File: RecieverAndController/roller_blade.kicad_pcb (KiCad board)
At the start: 2 copper layers, 57 x 60.4 mm, 2 parts

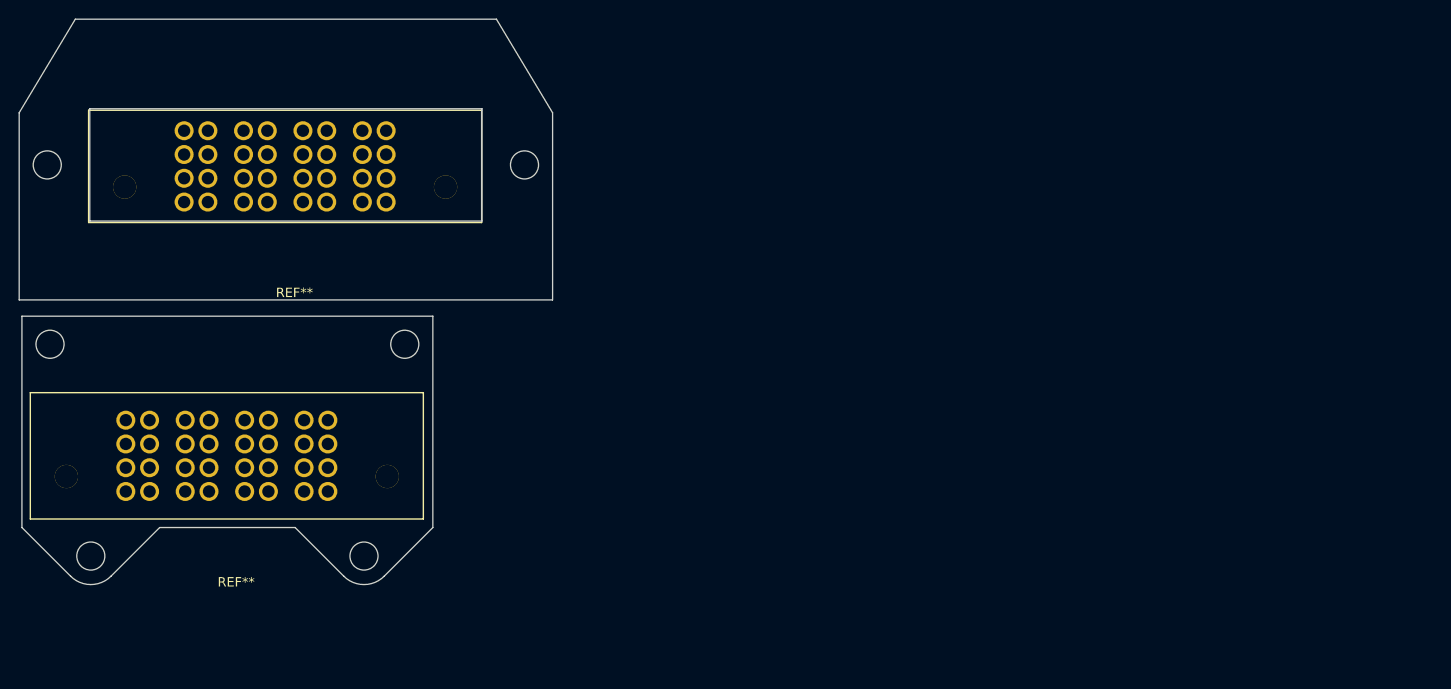
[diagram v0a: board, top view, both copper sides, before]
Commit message: adding footprints to schematic
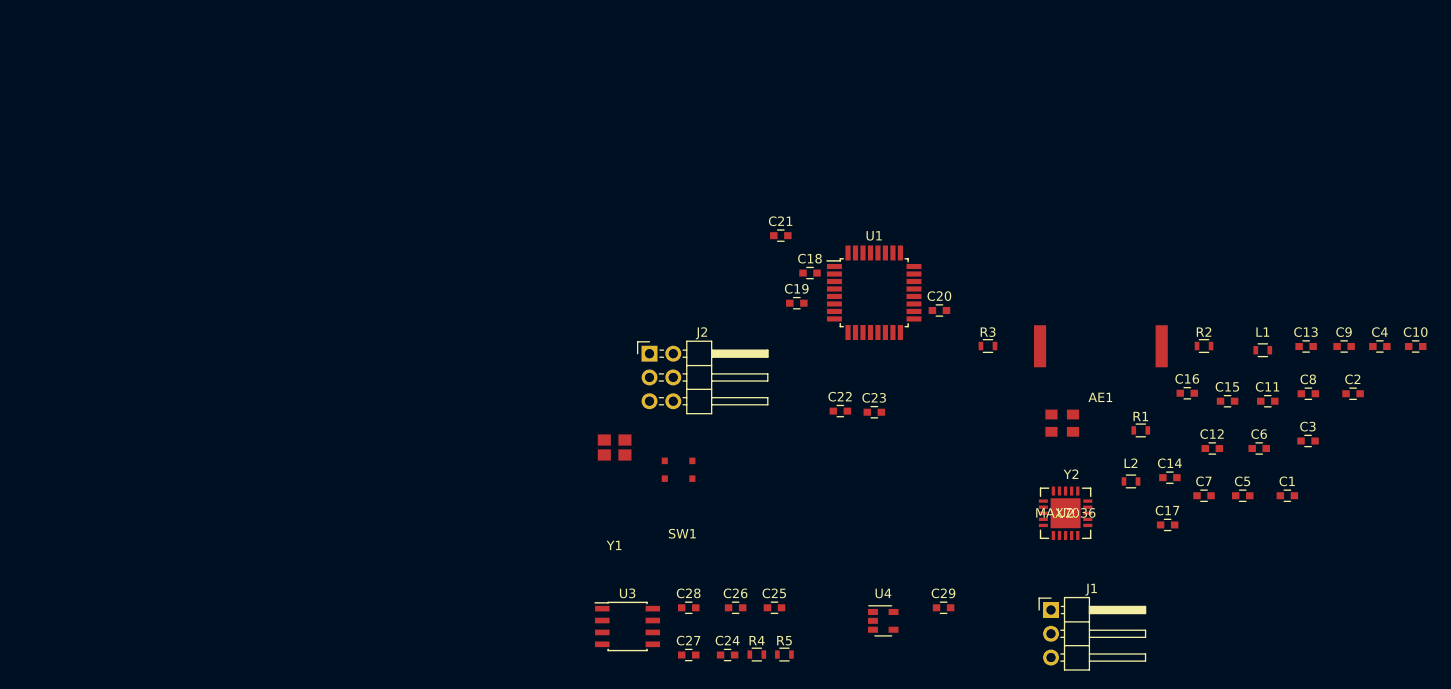
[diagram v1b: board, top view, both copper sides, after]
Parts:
- removed REF** (x2): PES-04-01-S-VT, Custom:PES-04-01-S-VT
- added AE1: Antenna, Custom:311-1570-1-ND, F.Cu at (218.1, 101.6)
- added C1: 4.7pF, Capacitors_SMD:C_0603, F.Cu at (238.0, 117.6)
- added C10: 10pF, Capacitors_SMD:C_0603, F.Cu at (251.8, 101.7)
- added C11: .1uF, Capacitors_SMD:C_0603, F.Cu at (235.9, 107.5)
- added C12: 220pF, Capacitors_SMD:C_0603, F.Cu at (230.0, 112.6)
- added C13: 10pF, Capacitors_SMD:C_0603, F.Cu at (240.0, 101.7)
- added C14: 10pF, Capacitors_SMD:C_0603, F.Cu at (225.5, 115.7)
- added C15: 100pF, Capacitors_SMD:C_0603, F.Cu at (231.6, 107.5)
- added C16: .1uF, Capacitors_SMD:C_0603, F.Cu at (227.3, 106.7)
- added C17: .1uF, Capacitors_SMD:C_0603, F.Cu at (225.2, 120.7)
- added C18: 100nF, Capacitors_SMD:C_0603, F.Cu at (187.0, 93.8)
- added C19: 100nF, Capacitors_SMD:C_0603, F.Cu at (185.6, 97.0)
- added C2: 100pF, Capacitors_SMD:C_0603, F.Cu at (245.1, 106.7)
- added C20: 100nF, Capacitors_SMD:C_0603, F.Cu at (200.9, 97.8)
- added C21: 100nF, Capacitors_SMD:C_0603, F.Cu at (183.9, 89.8)
- added C22: 18pF, Capacitors_SMD:C_0603, F.Cu at (190.3, 108.6)
- added C23: 18pF, Capacitors_SMD:C_0603, F.Cu at (193.9, 108.7)
- added C24: 1nF, Capacitors_SMD:C_0603, F.Cu at (178.2, 134.6)
- added C25: 1nF, Capacitors_SMD:C_0603, F.Cu at (183.2, 129.6)
- added C26: 100nF, Capacitors_SMD:C_0603, F.Cu at (179.1, 129.6)
- added C27: 100nF, Capacitors_SMD:C_0603, F.Cu at (174.1, 134.6)
- added C28: 100nF, Capacitors_SMD:C_0603, F.Cu at (174.1, 129.6)
- added C29: 1uF, Capacitors_SMD:C_0603, F.Cu at (201.3, 129.6)
- added C3: 100pF, Capacitors_SMD:C_0603, F.Cu at (240.2, 111.8)
- added C4: .1uF, Capacitors_SMD:C_0603, F.Cu at (247.9, 101.7)
- added C5: 390pF, Capacitors_SMD:C_0603, F.Cu at (233.3, 117.6)
- added C6: 180pF, Capacitors_SMD:C_0603, F.Cu at (235.0, 112.6)
- added C7: 1uF, Capacitors_SMD:C_0603, F.Cu at (229.1, 117.6)
- added C8: .01uF, Capacitors_SMD:C_0603, F.Cu at (240.3, 106.7)
- added C9: 22pF, Capacitors_SMD:C_0603, F.Cu at (244.1, 101.7)
- added J1: Conn_01x03, Pin_Headers:Pin_Header_Angled_1x03_Pitch2.54mm, F.Cu at (212.8, 129.8)
- added J2: Conn_02x03_Counter_Clockwise, Pin_Headers:Pin_Header_Angled_2x03_Pitch2.54mm, F.Cu at (169.9, 102.4)
- added L1: 100nH, Inductors_SMD:L_0603, F.Cu at (235.4, 102.1)
- added L2: 27nH, Inductors_SMD:L_0603, F.Cu at (221.3, 116.1)
- added R1: 22kOHM, Resistors_SMD:R_0603, F.Cu at (222.4, 110.6)
- added R2: 220kOhm, Resistors_SMD:R_0603, F.Cu at (229.1, 101.6)
- added R3: 10k, Resistors_SMD:R_0603, F.Cu at (206.0, 101.6)
- added R4: 10, Resistors_SMD:R_0603, F.Cu at (181.3, 134.6)
- added R5: 50, Resistors_SMD:R_0603, F.Cu at (184.3, 134.6)
- added SW1: SW_DIP_x01, Custom:CKN10291CT-ND, F.Cu at (173.0, 114.8)
- added U1: ATMEGA328-AU, Housings_QFP:TQFP-32_7x7mm_Pitch0.8mm, F.Cu at (193.9, 95.9)
- added U2: MAX7036, Custom:MAX7036GTP, F.Cu at (214.3, 119.5)
- added U3: MLX90365, Housings_SOIC:SOIC-8_3.9x4.9mm_Pitch1.27mm, F.Cu at (167.5, 131.6)
- added U4: AP2204_3V3, TO_SOT_Packages_SMD:SOT-23-5, F.Cu at (194.9, 131.0)
- added Y1: 16MHz, Custom:SER3686DKR-ND, F.Cu at (166.2, 112.5)
- added Y2: 13.56MHz, Custom:1253-1737-1-ND, F.Cu at (214.0, 109.9)
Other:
- board outline removed
- rule pad_to_mask_clearance: 0.2 -> 0
